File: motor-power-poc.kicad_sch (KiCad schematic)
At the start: 0 parts

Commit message: schem: import ESP32-S3 and USBC from adbq-usb-temp
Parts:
- added AE1: Antenna, RF_Antenna:Johanson_2450AT18x100, symbol Device:Antenna
- added C1, C14, C15, C9: 1u, Capacitor_SMD:C_0402_1005Metric, symbol Device:C
- added C10, C11, C16, C17, C18: 0u1, Capacitor_SMD:C_0402_1005Metric, symbol Device:C
- added C13: 10n, Capacitor_SMD:C_0402_1005Metric, symbol Device:C
- added C23, C25: 12p, Capacitor_SMD:C_0402_1005Metric, symbol Device:C
- added C28, C29: 1p2, Capacitor_SMD:C_0402_1005Metric, symbol Device:C
- added C52: 1p, Capacitor_SMD:C_0402_1005Metric, symbol Device:C
- added C8: 10u, Capacitor_SMD:C_0402_1005Metric, symbol Device:C
- added D1, D2, D3: H5VU10U, Pers:Diode_DFN1006, symbol Pers:H5VU10U
- added D7: D_Schottky, Diode_SMD:D_SMA, symbol Device:D_Schottky
- added J4: USB_C_Receptacle_USB2.0_14P, Connector_USB:USB_C_Receptacle_HRO_TYPE-C-31-M-12, symbol Connector:USB_C_Receptacle_USB2.0_14P
- added JP1: Jumper_2_Open, Jumper:SolderJumper-2_P1.3mm_Open_RoundedPad1.0x1.5mm, symbol Jumper:Jumper_2_Open
- added L2, L4, L7: 2n7, Inductor_SMD:L_0402_1005Metric, symbol Device:L
- added L3: 24n, Inductor_SMD:L_0402_1005Metric, symbol Device:L
- added L6: 3n9, Inductor_SMD:L_0402_1005Metric, symbol Device:L
- added R1, R2, R3: 10k, Resistor_SMD:R_0402_1005Metric, symbol Device:R
- added R10, R14: 22, Resistor_SMD:R_0402_1005Metric, symbol Device:R
- added R12, R13: 5k1, Resistor_SMD:R_0402_1005Metric, symbol Device:R
- added R25, R26: 20k, Resistor_SMD:R_0402_1005Metric, symbol Device:R
- added SW1, SW2: SW_Push, Button_Switch_SMD:SW_SPST_TS-1088-xR020, symbol Switch:SW_Push
- added U1: ESP32-S3FH4R2, Package_DFN_QFN:QFN-56-1EP_7x7mm_P0.4mm_EP5.6x5.6mm, symbol PCM_Espressif:ESP32-S3
- added Y1: 48M, Crystal:Crystal_SMD_2016-4Pin_2.0x1.6mm, symbol Device:Crystal_GND24
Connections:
- new net: J4.A5 (CC1), R12.2
- new net: J4.B5 (CC2), R13.2
- new net: C52.2, L6.2, L7.2
- new net: JP1.2 (B), R3.2
- new net: C1.1, R1.2, U1.4 (CHIP_PU/RESET)
- new net: JP1.1 (A), U1.52 (GPIO46)
- new net +3V3: C10.1, C13.1, C14.1, C17.1, C18.1, C8.1, L2.1, R1.1, R2.2, R25.1, R26.1, U1.20 (VDD3P3_RTC), U1.46 (VDD3P3_CPU), U1.55 (VDDA), U1.56 (VDDA)
- new net +5V: D7.1 (K)
- new net BOOT: R2.1, U1.5 (GPIO0/BOOT)
- new net BOOT/SCL: SW1.2
- new net CHIP_PU: SW2.2
- new net D+: D2.1 (K), J4.A6 (D+), J4.B6 (D+), R10.2
- new net D-: D1.1 (K), J4.A7 (D-), J4.B7 (D-), R14.2
- new net ESP_D+: R10.1, U1.26 (GPIO20/USB_D+/ADC2_CH9)
- new net ESP_D-: R14.1, U1.25 (GPIO19/USB_D-/ADC2_CH8)
- new net GND: C1.2, C10.2, C11.2, C13.2, C14.2, C15.2, C16.2, C17.2, C18.2, C23.1, C25.2, C28.2, C29.2, C8.2, C9.2, D1.2 (A), D2.2 (A), D3.2 (A), J4.A1 (GND), J4.A12 (GND), J4.B1 (GND), J4.B12 (GND), J4.S1 (SHIELD), L7.1, R12.1, R13.1, R3.1, SW1.1, SW2.1, U1.57 (GND), Y1.2, Y1.4
- new net RF_ANT: AE1.1 (A), L6.1
- new net RF_ESP: C28.1, L4.2, U1.1 (LNA_IN/RF)
- new net RF_TRANS: C29.1, C52.1, L4.1
- new net SCL: R25.2, U1.7 (GPIO2/ADC1_CH1)
- new net SDA: R26.2, U1.8 (GPIO3/ADC1_CH2)
- new net VBUS: D3.1 (K), D7.2 (A), J4.A4 (VBUS), J4.A9 (VBUS), J4.B4 (VBUS), J4.B9 (VBUS)
- new net VDD3P3: C11.1, L2.2, U1.2 (VDD3P3), U1.3 (VDD3P3)
- new net VDD_SPI: C15.1, C16.1, U1.29 (VDD_SPI)
- new net XTAL_N: C25.1, U1.53 (XTAL_N), Y1.3
- new net XTAL_P: L3.1, U1.54 (XTAL_P)
- new net XTAL_PL: C23.2, L3.2, Y1.1
- no-connect marks 0 -> 13
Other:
- note added: "Buttons"
- note added: "EN RC delay"
- note added: "HSE"
- note added: "USB/ESP"

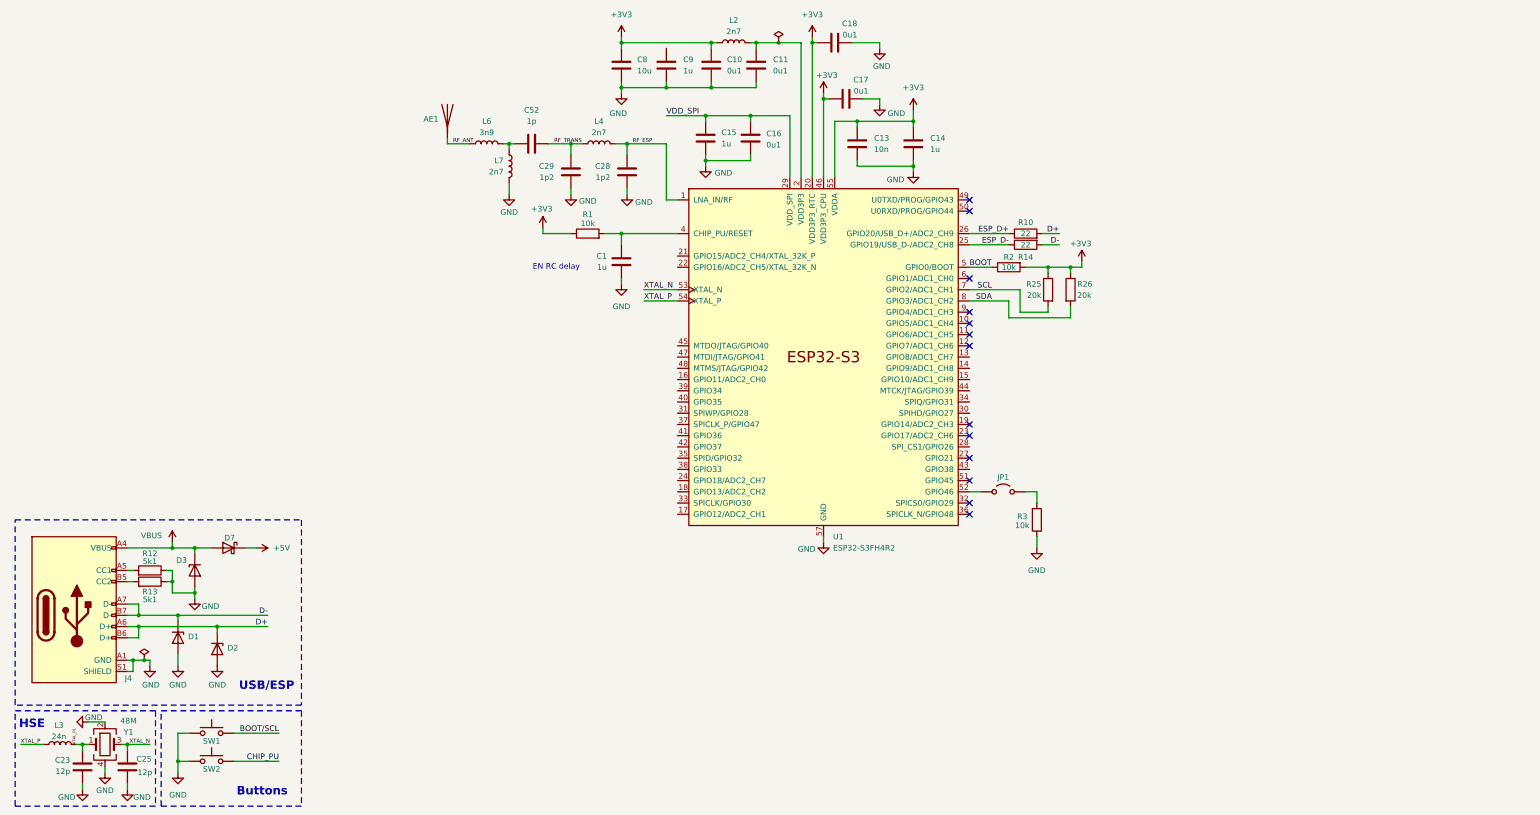
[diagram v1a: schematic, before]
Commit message: schem: add TPS5430 5v SMPS with calculations note
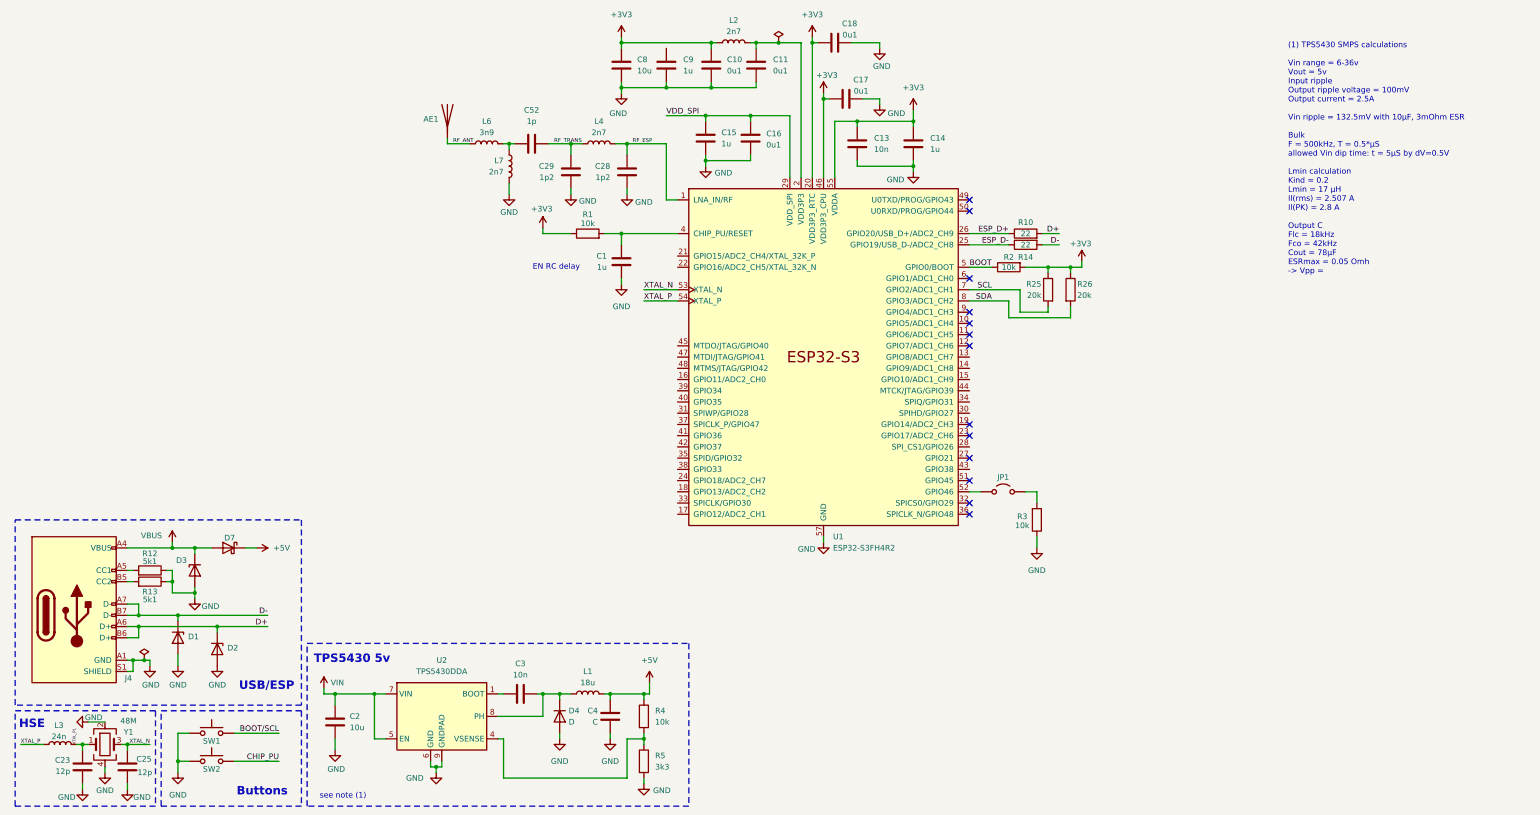
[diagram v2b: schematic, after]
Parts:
- added C2: 10u, symbol Device:C
- added C3: 10n, symbol Device:C
- added C4: C, symbol Device:C
- added D4: D, symbol Device:D
- added L1: 18u, symbol Device:L
- added R4: 10k, symbol Device:R
- added R5: 3k3, symbol Device:R
- added U2: TPS5430DDA, Package_SO:TI_SO-PowerPAD-8_ThermalVias, symbol Regulator_Switching:TPS5430DDA
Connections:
- net +5V: now also C4.1, L1.2, R4.1
- net GND: now also C2.2, C4.2, D4.2 (A), R5.2, U2.6 (GND), U2.9 (GNDPAD)
- new net: C3.2, D4.1 (K), L1.1, U2.8 (PH)
- new net: C3.1, U2.1 (BOOT)
- new net: R4.2, R5.1, U2.4 (VSENSE)
- new net VIN: C2.1, U2.5 (EN), U2.7 (VIN)
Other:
- note added: "TPS5430 5v"
- note added: "see note (1)"

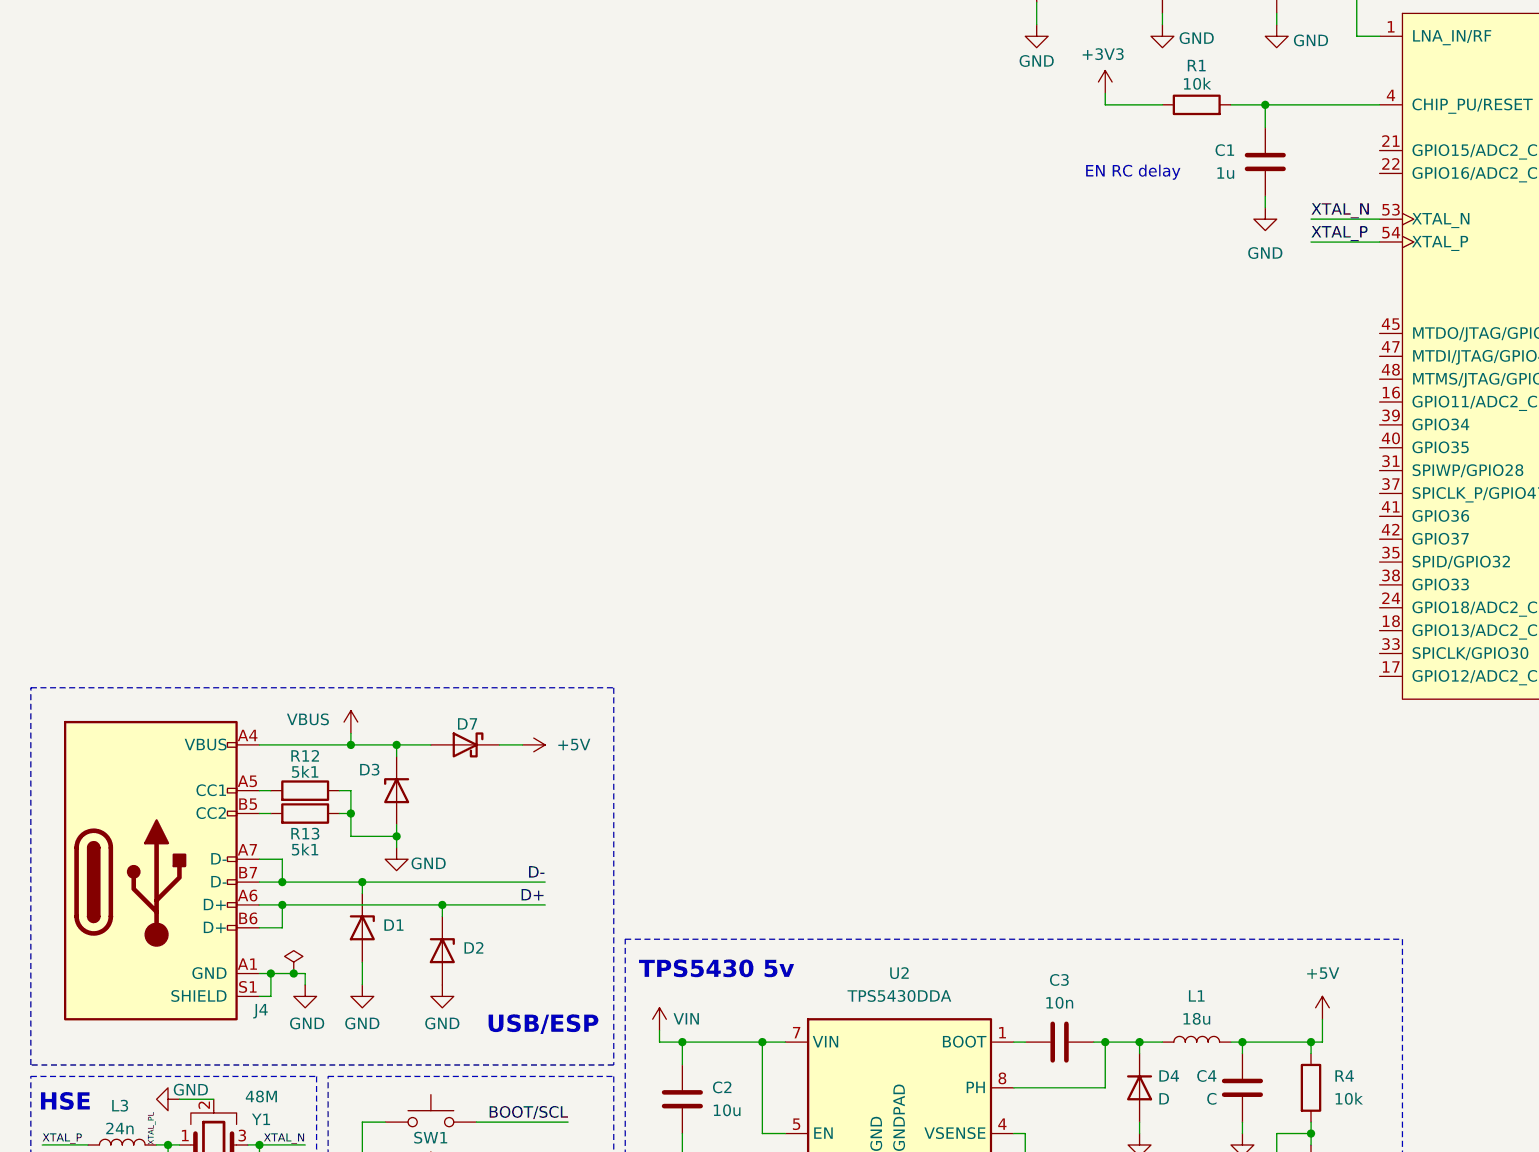
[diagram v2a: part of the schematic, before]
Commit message: schem: add TPS2121 5v power mux
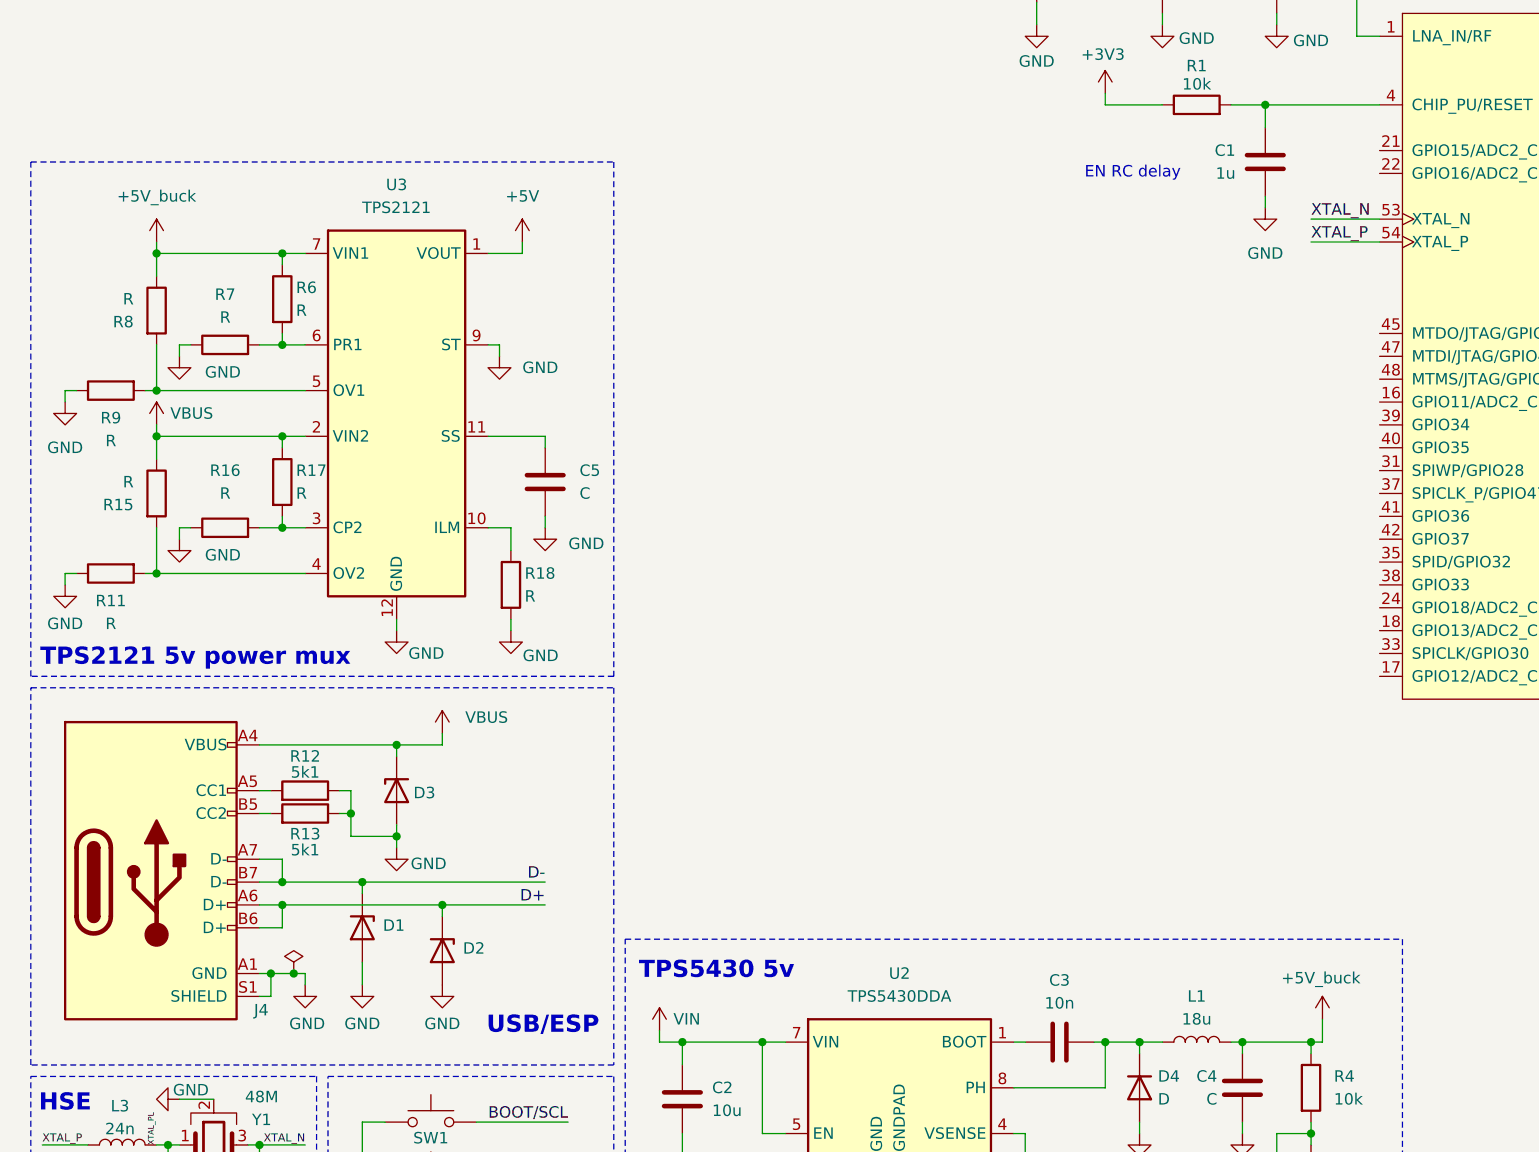
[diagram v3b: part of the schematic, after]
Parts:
- removed D7: D_Schottky, Diode_SMD:D_SMA, symbol Device:D_Schottky
- added C5: C, symbol Device:C
- added R11, R15, R16, R17, R18, R6, R7, R8, R9: R, symbol Device:R
- added U3: TPS2121, Package_DFN_QFN:Texas_VQFN-HR-12_2x2.5mm_P0.5mm_ThermalVias, symbol Pers:TPS2121
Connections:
- net +5V: now also U3.1 (VOUT), U3.8 (VOUT); no longer C4.1, L1.2, R4.1
- net GND: now also C5.2, R11.1, R16.1, R18.2, R7.1, R9.1, U3.12 (GND), U3.9 (ST)
- net VBUS: now also R15.1, R17.1, U3.2 (VIN2)
- new net: R6.2, R7.2, U3.6 (PR1)
- new net: R18.1, U3.10 (ILM)
- new net: C5.1, U3.11 (SS)
- new net: R16.2, R17.2, U3.3 (CP2)
- new net: R11.2, R15.2, U3.4 (OV2)
- new net: R8.2, R9.2, U3.5 (OV1)
- new net +5V_buck: C4.1, L1.2, R4.1, R6.1, R8.1, U3.7 (VIN1)
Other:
- note added: "TPS2121 5v power mux"

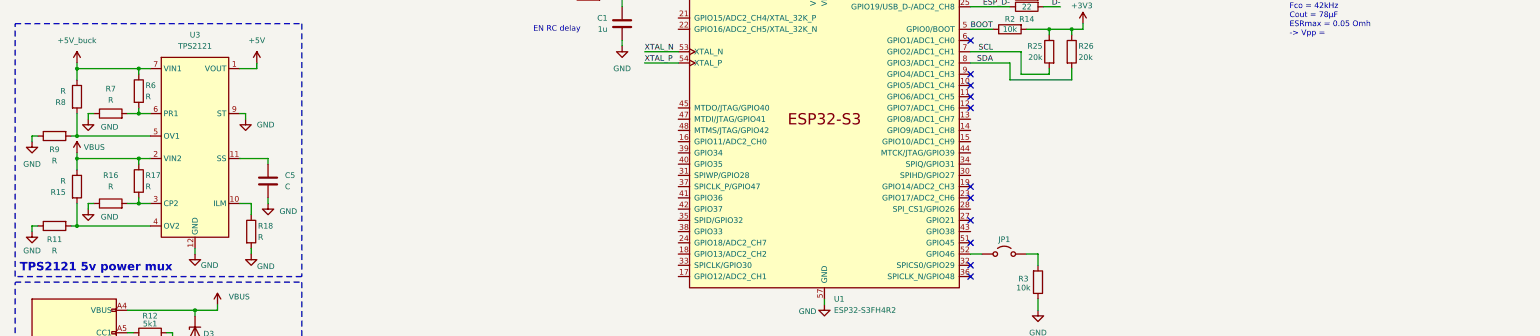
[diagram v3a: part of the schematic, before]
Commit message: schem: add TPS2121 5v power mux components values
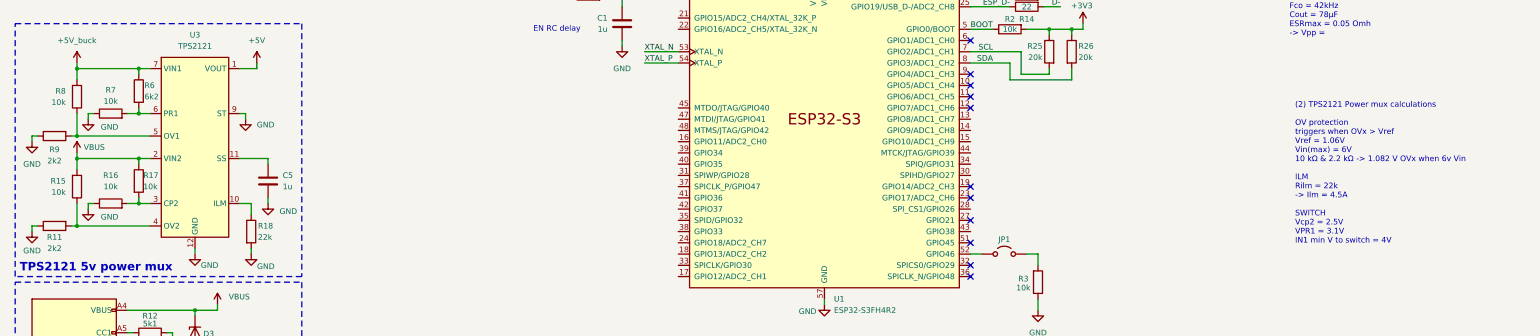
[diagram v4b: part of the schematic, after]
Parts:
- C5: value C -> 1u
- R11, R9: value R -> 2k2
- R15, R16, R17, R7, R8: value R -> 10k
- R18: value R -> 22k
- R6: value R -> 6k2
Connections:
- net +5V_buck: now also R8.2; no longer R8.1
- net VBUS: now also R15.2; no longer R15.1
- net at R11.2, U3.4 (OV2): now also R15.1; no longer R15.2
- net at R9.2, U3.5 (OV1): now also R8.1; no longer R8.2
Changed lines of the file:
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@@
 		)
 	)
+	(text_box "(2) TPS2121 Power mux calculations\n\nOV protection\ntriggers when OVx > Vref\nVref = 1.06V\nVin(max) = 6V\n10 kΩ & 2.2 kΩ -> 1.082 V OVx when 6v Vin\n\nILM\nRilm = 22k\n-> Ilm = 4.5A\n\nSWITCH\nVcp2 = 2.5V\nVPR1 = 3.1V\nIN1 min V to switch = 4V"
+		(exclude_from_sim no)
+		(at 304.8 87.63 0)
+		(size 69.85 55.88)
+		(margins 0.9525 0.9525 0.9525 0.9525)
+		(stroke
+			(width -0.0001)
+			(type solid)
+		)
+		(fill
+			(type none)
+		)
+		(effects
+			(font
+				(size 1.27 1.27)
+			)
+			(justify left top)
+		)
+	)
 	(junction
 		(at 44.45 101.6)
@@
 		(dnp no)
 		(property "Reference" "R6"
-			(at 45.974 85.09 0)
+			(at 45.72 85.09 0)
 			(effects
 				(font
@@
 			)
 		)
-		(property "Value" "R"
-			(at 45.974 87.63 0)
+		(property "Value" "6k2"
+			(at 45.72 87.63 0)
 			(effects
 				(font
@@
 		(dnp no)
 		(property "Reference" "R11"
-			(at 25.4 119.888 90)
+			(at 25.4 119.38 90)
 			(effects
 				(font
@@
 			)
 		)
-		(property "Value" "R"
-			(at 25.4 122.428 90)
+		(property "Value" "2k2"
+			(at 25.4 121.92 90)
 			(effects
 				(font
@@
 			)
 		)
-		(property "Value" "R"
+		(property "Value" "10k"
 			(at 38.1 107.95 90)
 			(effects
@@
 		(lib_id "Device:R")
 		(at 30.48 87.63 0)
+		(mirror x)
 		(unit 1)
 		(exclude_from_sim no)
@@
 		(on_board yes)
 		(dnp no)
-		(fields_autoplaced yes)
 		(property "Reference" "R8"
-			(at 27.94 88.9001 0)
+			(at 27.94 86.3599 0)
 			(effects
 				(font
@@
 			)
 		)
-		(property "Value" "R"
-			(at 27.94 86.3601 0)
+		(property "Value" "10k"
+			(at 27.94 88.8999 0)
 			(effects
 				(font
@@
 		(lib_id "Device:R")
 		(at 30.48 107.95 0)
+		(mirror x)
 		(unit 1)
 		(exclude_from_sim no)
@@
 		(on_board yes)
 		(dnp no)
-		(fields_autoplaced yes)
 		(property "Reference" "R15"
-			(at 27.94 109.2201 0)
+			(at 27.94 106.6799 0)
 			(effects
 				(font
@@
 			)
 		)
-		(property "Value" "R"
-			(at 27.94 106.6801 0)
+		(property "Value" "10k"
+			(at 27.94 109.2199 0)
 			(effects
 				(font
@@
 			)
 		)
-		(property "Value" "R"
+		(property "Value" "2k2"
 			(at 25.4 102.108 90)
 			(effects
@@
 		(dnp no)
 		(property "Reference" "R17"
-			(at 45.974 105.41 0)
+			(at 45.466 105.41 0)
 			(effects
 				(font
@@
 			)
 		)
-		(property "Value" "R"
-			(at 45.974 107.95 0)
+		(property "Value" "10k"
+			(at 45.466 107.95 0)
 			(effects
 				(font
@@
 			)
 		)
-		(property "Value" "R"
+		(property "Value" "22k"
 			(at 71.374 119.38 0)
 			(effects
@@
 		(on_board yes)
 		(dnp no)
-		(fields_autoplaced yes)
 		(property "Reference" "C5"
-			(at 77.47 105.4099 0)
+			(at 76.962 105.41 0)
 			(effects
 				(font
@@
 			)
 		)
-		(property "Value" "C"
-			(at 77.47 107.9499 0)
+		(property "Value" "1u"
+			(at 76.962 107.95 0)
 			(effects
 				(font
@@
 		(dnp no)
 		(property "Reference" "R7"
-			(at 38.1 85.852 90)
+			(at 38.1 86.106 90)
 			(effects
 				(font
@@
 			)
 		)
-		(property "Value" "R"
-			(at 38.1 88.392 90)
+		(property "Value" "10k"
+			(at 38.1 88.646 90)
 			(effects
 				(font
